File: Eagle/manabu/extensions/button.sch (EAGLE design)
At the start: 5 parts

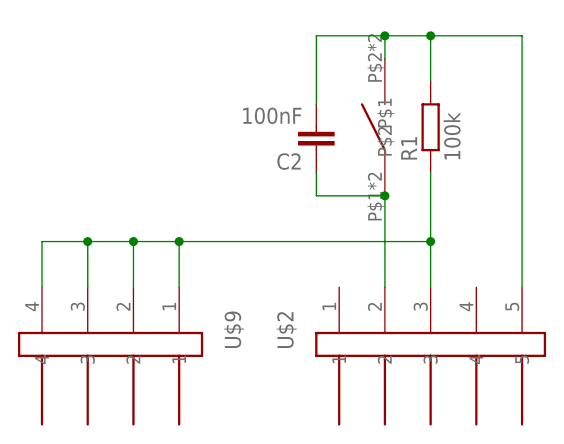
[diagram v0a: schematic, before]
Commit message: added button 12x12 and then used in button extension
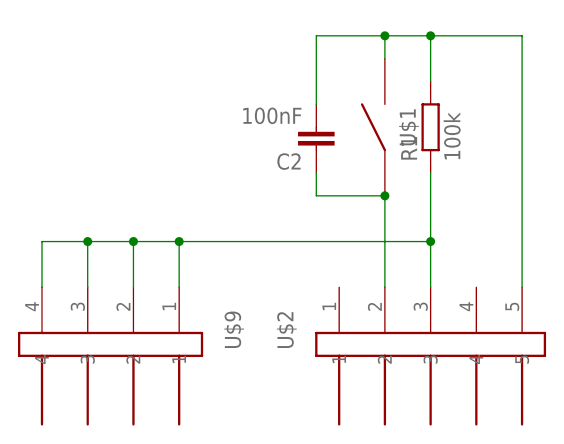
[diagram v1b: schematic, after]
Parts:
- U$1: value BUTTON_6.3X6.3 -> BUTTON_7X7; device !stavebnice03:BUTTON_6.3X6.3 -> !stavebnice03:BUTTON_7X7
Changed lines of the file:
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@@
 <?xml version="1.0" encoding="utf-8"?>
 <!DOCTYPE eagle SYSTEM "eagle.dtd">
-<eagle version="7.2.0">
+<eagle version="7.4.0">
 <drawing>
 <settings>
@@
 <part name="U$9" library="!stavebnice03" deviceset="JUMPER4M" device=""/>
 <part name="R1" library="resistor" deviceset="R-EU_" device="R0603" value="100k"/>
-<part name="U$1" library="!stavebnice03" deviceset="BUTTON_6.3X6.3" device=""/>
 <part name="U$2" library="!stavebnice03" deviceset="JUMPER5M" device=""/>
 <part name="C2" library="resistor" deviceset="C-EU" device="C0603K" value="100nF"/>
+<part name="U$1" library="!stavebnice03" deviceset="BUTTON_7X7" device=""/>
 </parts>
 <sheets>
@@
 <instance part="U$9" gate="G$1" x="137.16" y="27.94" rot="R270"/>
 <instance part="R1" gate="G$1" x="172.72" y="53.34" rot="R90"/>
-<instance part="U$1" gate="G$1" x="167.64" y="53.34" rot="R90"/>
 <instance part="U$2" gate="G$1" x="172.72" y="27.94" rot="MR270"/>
 <instance part="C2" gate="G$1" x="160.02" y="50.8" rot="R180"/>
+<instance part="U$1" gate="G$1" x="167.64" y="53.34" rot="R90"/>
 </instances>
 <busses>
@@
 <net name="AA" class="0">
 <segment>
-<pinref part="U$1" gate="G$1" pin="P$2"/>
 <wire x1="160.02" y1="63.5" x2="167.64" y2="63.5" width="0.1524" layer="91"/>
 <wire x1="167.64" y1="63.5" x2="167.64" y2="60.96" width="0.1524" layer="91"/>
@@
 <wire x1="182.88" y1="63.5" x2="182.88" y2="35.56" width="0.1524" layer="91"/>
 <junction x="172.72" y="63.5"/>
+<pinref part="U$1" gate="G$1" pin="P$2"/>
 </segment>
 </net>
@@
 <pinref part="C2" gate="G$1" pin="1"/>
 <wire x1="160.02" y1="48.26" x2="160.02" y2="45.72" width="0.1524" layer="91"/>
-<pinref part="U$1" gate="G$1" pin="P$1"/>
 <wire x1="167.64" y1="35.56" x2="167.64" y2="45.72" width="0.1524" layer="91"/>
 <pinref part="U$2" gate="G$1" pin="2"/>
 <wire x1="160.02" y1="45.72" x2="167.64" y2="45.72" width="0.1524" layer="91"/>
+<pinref part="U$1" gate="G$1" pin="P$1"/>
 <junction x="167.64" y="45.72"/>
 </segment>
